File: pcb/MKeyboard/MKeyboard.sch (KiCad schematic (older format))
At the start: 67 parts, among them J1 USB_C_Receptacle_USB2.0, SW0 SW_Push, SW1 SW_Push, SW10 SW_Push, SW11 SW_Push, SW12 SW_Push, SW2 SW_Push, SW20 SW_Push, SW21 SW_Push, SW22 SW_Push, SW30 SW_Push, SW31 SW_Push, SW32 SW_Push, SW40 SW_Push, SW41 SW_Push, SW42 SW_Push, U1 AT90USB646-AU, Y1 16MHz

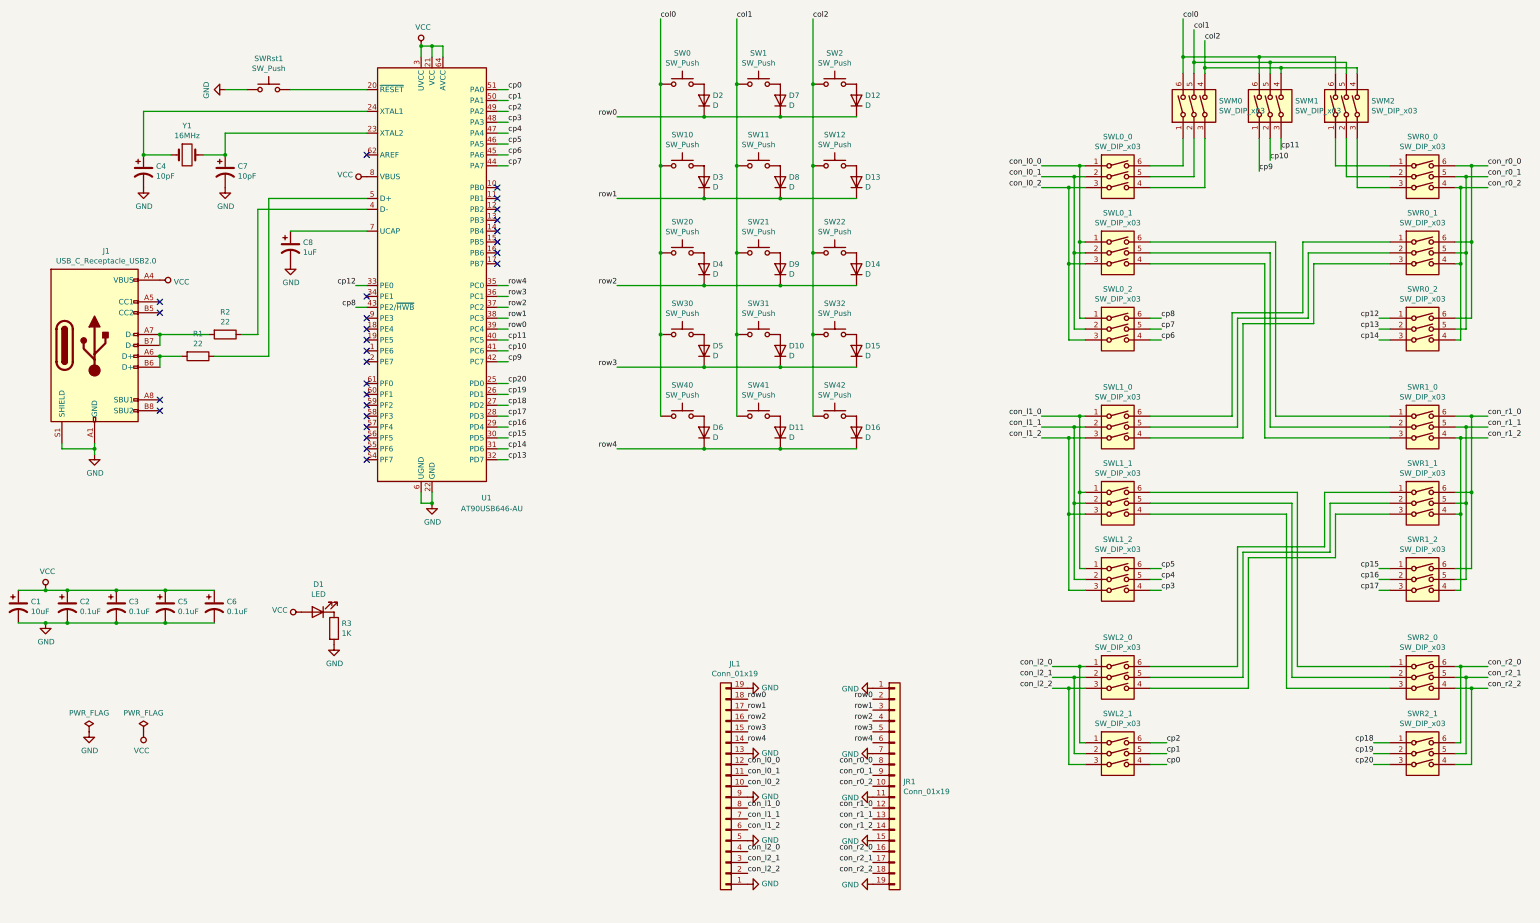
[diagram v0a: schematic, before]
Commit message: 0-ohm resisters instead of dip-switches, component placement in PCB layout.
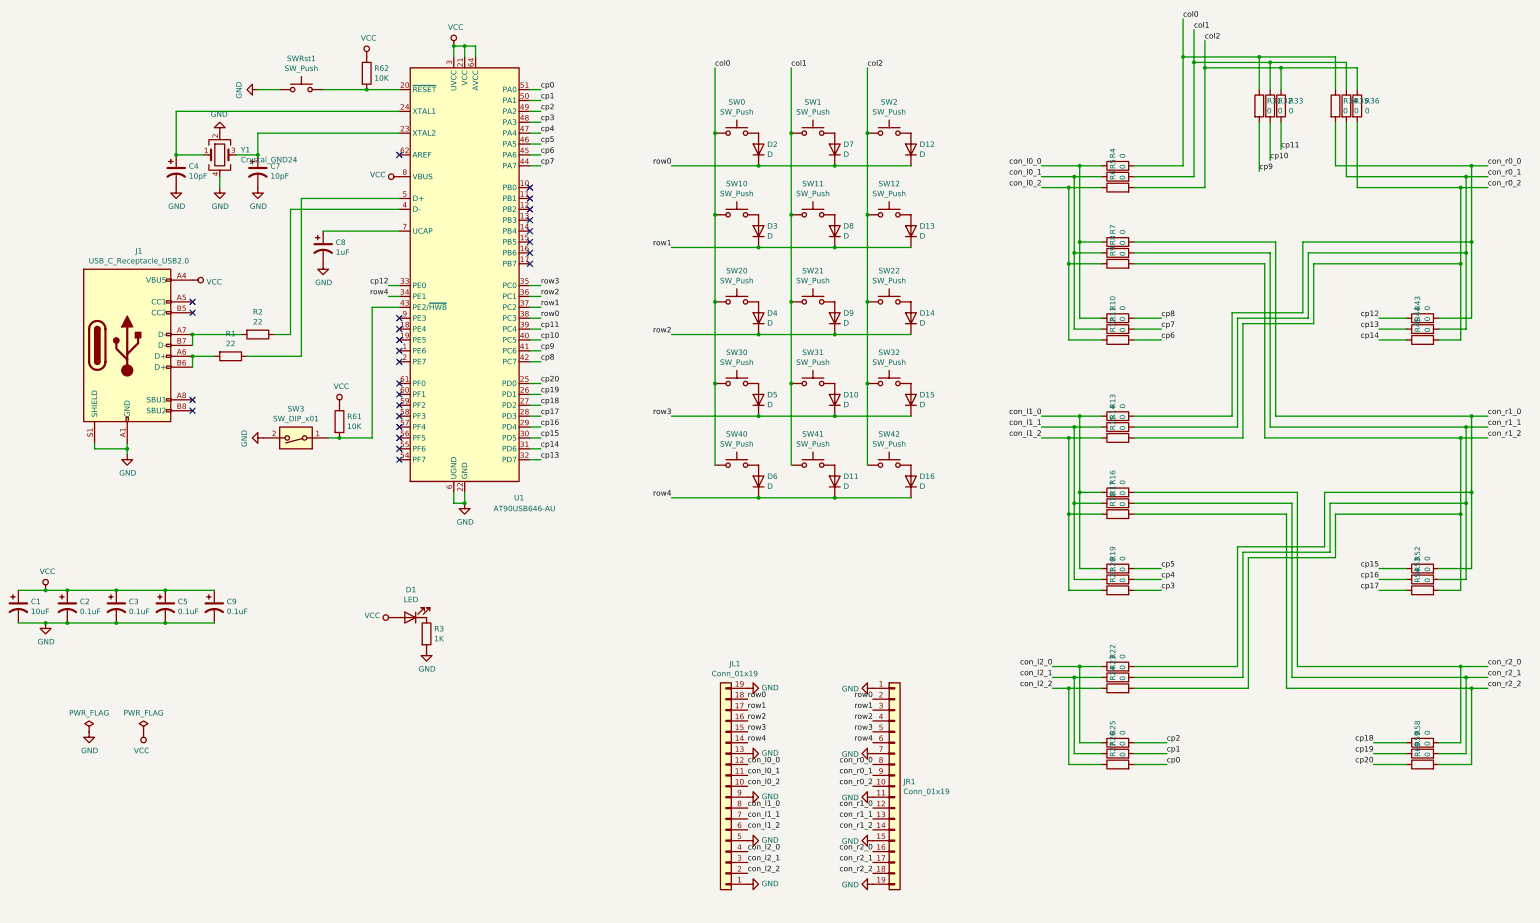
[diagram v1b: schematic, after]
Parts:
- removed C6: 0.1uF, symbol Device:CP1
- removed SWL0_0, SWL0_1, SWL0_2, SWL1_0, SWL1_1, SWL1_2, SWL2_0, SWL2_1, SWM0, SWM1, SWM2, SWR0_0, SWR0_1, SWR0_2, SWR1_0, SWR1_1, SWR1_2, SWR2_0, SWR2_1: SW_DIP_x03, symbol Switch:SW_DIP_x03
- removed Y1: 16MHz, symbol Device:Crystal
- added C9: 0.1uF, Capacitor_SMD:C_1206_3216Metric_Pad1.42x1.75mm_HandSolder, symbol Device:CP1
- added R10, R11, R12, R13, R14, R15, R16, R17, R18, R19, R20, R21, R22, R23, R24, R25, R26, R27, R31, R32, R33, R34, R35, R36, R4, R43, R44, R45, R5, R52, R53, R54, R58, R59, R6, R60, R7, R8, R9: 0, Resistor_SMD:R_1206_3216Metric_Pad1.42x1.75mm_HandSolder, symbol Device:R
- added R61, R62: 10K, Resistor_SMD:R_1206_3216Metric_Pad1.42x1.75mm_HandSolder, symbol Device:R
- added SW3: SW_DIP_x01, Button_Switch_SMD:SW_DIP_SPSTx01_Slide_6.7x4.1mm_W8.61mm_P2.54mm_LowProfile, symbol Switch:SW_DIP_x01
- added Y1: Crystal_GND24, Crystal:Crystal_SMD_7050-4Pin_7.0x5.0mm, symbol Device:Crystal_GND24
- C1, C2, C3, C4, C5, C7, C8: footprint (none) -> Capacitor_SMD:C_1206_3216Metric_Pad1.42x1.75mm_HandSolder
- D1: footprint (none) -> LED_SMD:LED_1206_3216Metric_Pad1.42x1.75mm_HandSolder
- D10, D11, D12, D13, D14, D15, D16, D2, D3, D4, D5, D6, D7, D8, D9: footprint (none) -> Diode_SMD:D_1206_3216Metric_Pad1.42x1.75mm_HandSolder
- J1: footprint (none) -> Connector_USB:USB_C_Receptacle_GCT_USB4085
- JL1: footprint (none) -> Connector_PinSocket_2.54mm:PinSocket_1x19_P2.54mm_Horizontal
- JR1: footprint (none) -> Connector_PinHeader_2.54mm:PinHeader_1x19_P2.54mm_Horizontal
- R1, R2, R3: footprint (none) -> Resistor_SMD:R_1206_3216Metric_Pad1.42x1.75mm_HandSolder
- SW0, SW1, SW10, SW11, SW12, SW2, SW20, SW21, SW22, SW30, SW31, SW32, SW40, SW41, SW42: footprint (none) -> Button_Switch_Keyboard:SW_Cherry_MX_1.00u_PCB
- SWRst1: footprint (none) -> Button_Switch_SMD:SW_Push_1P1T_NO_6x6mm_H9.5mm
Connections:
- net GND: now also C9.2, SW3.2, Y1.2, Y1.4
- net VCC: now also C9.1, R61.1, R62.1
- net col0: now also R31.1, R34.1, R4.2
- net col1: now also R32.1, R35.1, R5.2
- net col2: now also R33.1, R36.1, R6.2
- net con_l0_0: now also R10.1, R4.1, R7.1
- net con_l0_1: now also R11.1, R5.1, R8.1
- net con_l0_2: now also R12.1, R6.1, R9.1
- net con_l1_0: now also R13.1, R16.1, R19.1
- net con_l1_1: now also R14.1, R17.1, R20.1
- net con_l1_2: now also R15.1, R18.1, R21.1
- net con_l2_0: now also R22.1, R25.1
- net con_l2_1: now also R23.1, R26.1
- net con_l2_2: now also R24.1, R27.1
- net con_r0_0: now also R13.2, R34.2, R43.2
- net con_r0_1: now also R14.2, R35.2, R44.2
- net con_r0_2: now also R15.2, R36.2, R45.2
- net con_r1_0: now also R22.2, R52.2, R7.2
- net con_r1_1: now also R23.2, R53.2, R8.2
- net con_r1_2: now also R24.2, R54.2, R9.2
- net con_r2_0: now also R16.2, R58.2
- net con_r2_1: now also R17.2, R59.2
- net con_r2_2: now also R18.2, R60.2
- net cp0: now also R27.2
- net cp1: now also R26.2
- net cp10: now also U1.40 (PC5), R32.2; no longer U1.41 (PC6)
- net cp11: now also U1.39 (PC4), R33.2; no longer U1.40 (PC5)
- net cp12: now also R43.1
- net cp13: now also R44.1
- net cp14: now also R45.1
- net cp15: now also R52.1
- net cp16: now also R53.1
- net cp17: now also R54.1
- net cp18: now also R58.1
- net cp19: now also R59.1
- net cp2: now also R25.2
- net cp20: now also R60.1
- net cp3: now also R21.2
- net cp4: now also R20.2
- net cp5: now also R19.2
- net cp6: now also R12.2
- net cp7: now also R11.2
- net cp8: now also U1.42 (PC7), R10.2; no longer U1.43 (PE2/~HWB)
- net cp9: now also U1.41 (PC6), R31.2; no longer U1.42 (PC7)
- net row0: now also U1.38 (PC3); no longer U1.39 (PC4)
- net row1: now also U1.37 (PC2); no longer U1.38 (PC3)
- net row2: now also U1.36 (PC1); no longer U1.37 (PC2)
- net row3: now also U1.35 (PC0); no longer U1.36 (PC1)
- net row4: now also U1.34 (PE1); no longer U1.35 (PC0)
- net at SWRst1.2, U1.20 (~RESET): now also R62.2
- net at C7.1, U1.23 (XTAL2): now also Y1.3
- net at C4.1, U1.24 (XTAL1): now also Y1.1
- new net: R61.2, SW3.1, U1.43 (PE2/~HWB)
- no-connect marks 27 -> 26
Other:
- moved on the sheet: C4, C7, C8, D1, D10, D11, D12, D13, D14, D15, D16, D2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

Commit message: smaller components, positioning
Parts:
- C1, C2, C3, C4, C5, C7, C8, C9: footprint Capacitor_SMD:C_1206_3216Metric_Pad1.42x1.75mm_HandSolder -> Capacitor_SMD:C_0603_1608Metric_Pad1.05x0.95mm_HandSolder
- D1: footprint LED_SMD:LED_1206_3216Metric_Pad1.42x1.75mm_HandSolder -> LED_SMD:LED_0603_1608Metric_Pad1.05x0.95mm_HandSolder
- R1, R10, R11, R12, R13, R14, R15, R16, R17, R18, R19, R2, R20, R21, R22, R23, R24, R25, R26, R27, R3, R31, R32, R33, R34, R35, R36, R4, R43, R44, R45, R5, R52, R53, R54, R58, R59, R6, R60, R61, R62, R7, R8, R9: footprint Resistor_SMD:R_1206_3216Metric_Pad1.42x1.75mm_HandSolder -> Resistor_SMD:R_0603_1608Metric_Pad1.05x0.95mm_HandSolder
- Y1: footprint Crystal:Crystal_SMD_7050-4Pin_7.0x5.0mm -> Crystal:Crystal_SMD_0603-4Pin_6.0x3.5mm_HandSoldering

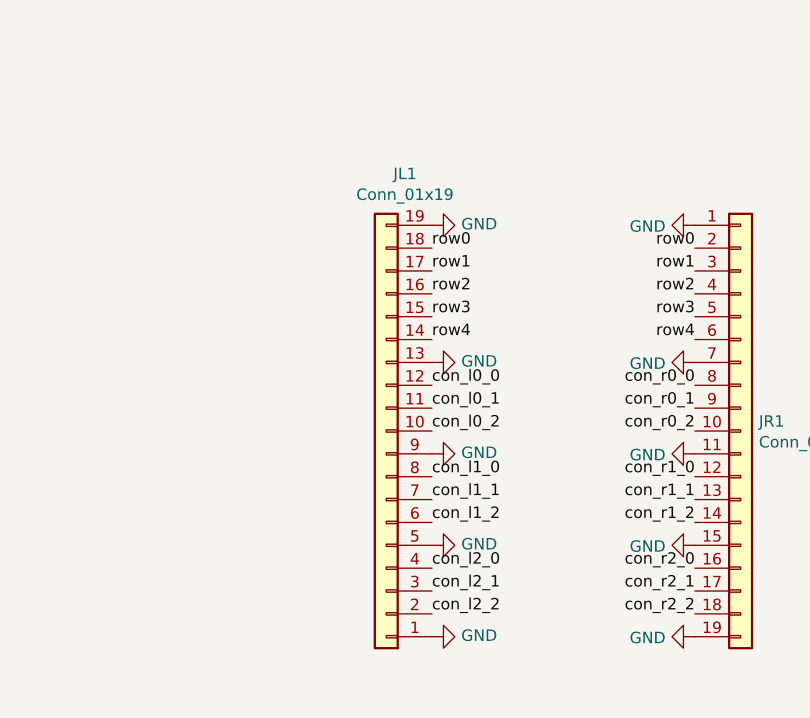
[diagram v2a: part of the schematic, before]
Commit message: fixed orientation of left connector
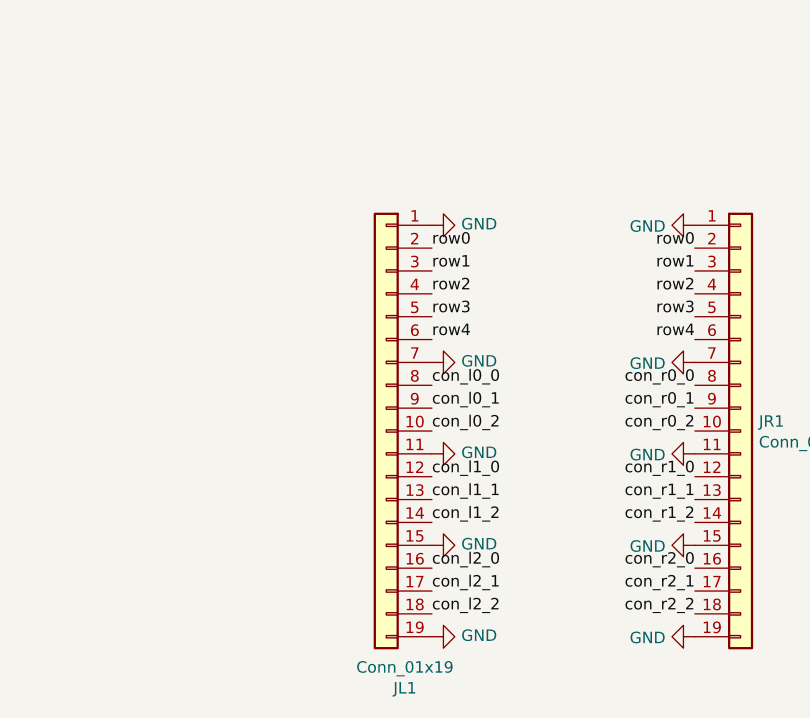
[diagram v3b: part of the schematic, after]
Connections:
- net GND: now also JL1.11 (Pin_11), JL1.15 (Pin_15), JL1.7 (Pin_7); no longer JL1.13 (Pin_13), JL1.5 (Pin_5), JL1.9 (Pin_9)
- net con_l0_0: now also JL1.8 (Pin_8); no longer JL1.12 (Pin_12)
- net con_l0_1: now also JL1.9 (Pin_9); no longer JL1.11 (Pin_11)
- net con_l1_0: now also JL1.12 (Pin_12); no longer JL1.8 (Pin_8)
- net con_l1_1: now also JL1.13 (Pin_13); no longer JL1.7 (Pin_7)
- net con_l1_2: now also JL1.14 (Pin_14); no longer JL1.6 (Pin_6)
- net con_l2_0: now also JL1.16 (Pin_16); no longer JL1.4 (Pin_4)
- net con_l2_1: now also JL1.17 (Pin_17); no longer JL1.3 (Pin_3)
- net con_l2_2: now also JL1.18 (Pin_18); no longer JL1.2 (Pin_2)
- net row0: now also JL1.2 (Pin_2); no longer JL1.18 (Pin_18)
- net row1: now also JL1.3 (Pin_3); no longer JL1.17 (Pin_17)
- net row2: now also JL1.4 (Pin_4); no longer JL1.16 (Pin_16)
- net row3: now also JL1.5 (Pin_5); no longer JL1.15 (Pin_15)
- net row4: now also JL1.6 (Pin_6); no longer JL1.14 (Pin_14)
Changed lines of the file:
@@
 cp20
-$Comp
-L Connector_Generic:Conn_01x19 JL1
-U 1 1 61C22FBA
-P 7850 8150
-F 0 "JL1" H 7768 7025 50  0000 C CNN
-F 1 "Conn_01x19" H 7768 7116 50  0000 C CNN
-F 2 "Connector_PinSocket_2.54mm:PinSocket_1x19_P2.54mm_Horizontal" H 7850 8150 50  0001 C CNN
-F 3 "~" H 7850 8150 50  0001 C CNN
-	1    7850 8150
-	-1   0    0    1
-$EndComp
 $Comp
 L Connector_Generic:Conn_01x19 JR1
@@
 Wire Wire Line
 	2700 6650 3150 6650
+$Comp
+L Connector_Generic:Conn_01x19 JL1
+U 1 1 61C22FBA
+P 7850 8150
+F 0 "JL1" H 7768 7025 50  0000 C CNN
+F 1 "Conn_01x19" H 7768 7116 50  0000 C CNN
+F 2 "Connector_PinSocket_2.54mm:PinSocket_1x19_P2.54mm_Horizontal" H 7850 8150 50  0001 C CNN
+F 3 "~" H 7850 8150 50  0001 C CNN
+	1    7850 8150
+	-1   0    0    -1
+$EndComp
 $EndSCHEMATC
